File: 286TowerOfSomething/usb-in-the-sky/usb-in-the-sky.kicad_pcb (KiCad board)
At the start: 2 copper layers, 105.8 x 65.9 mm, 27 parts, among them J1 Bus_ISA_8bit, J2 USB_A, SW1 SW_DIP_x05, U1 CH375, U2 74LS688, U3 74LS245, U4 74ALS688, U5 SST39SF010, U6 USBLC6-2SC6, Y1 12 MHz

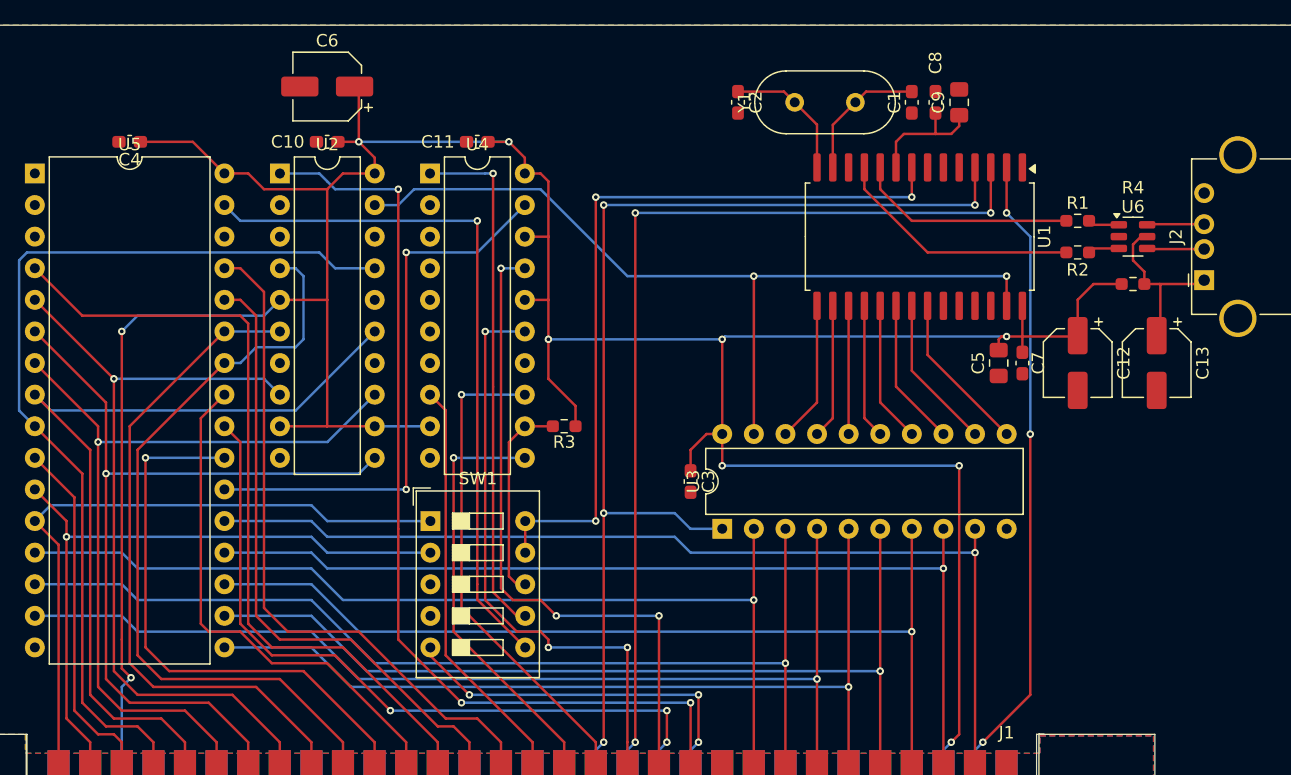
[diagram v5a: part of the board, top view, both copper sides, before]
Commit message: Work on USB in the Sky silkscreen
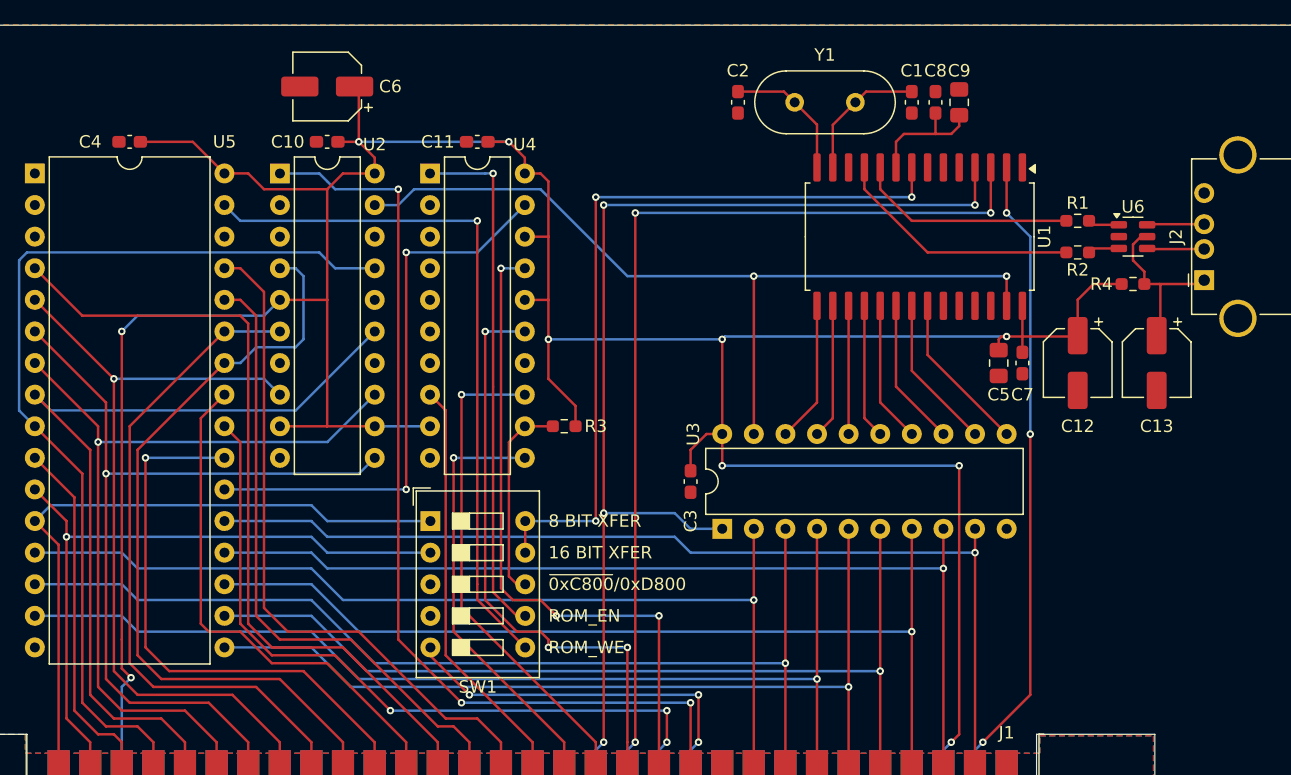
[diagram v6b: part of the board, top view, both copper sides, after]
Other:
- board text added: "16 BIT XFER"
- board text added: "8 BIT XFER"
- board text added: "ROM_EN"
- board text added: "ROM_WE"
- board text added: "~{0xC800}/0xD800"
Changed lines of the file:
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@@
 		(tags "capacitor electrolytic")
 		(property "Reference" "C12"
-			(at 0 -3.7 90)
+			(at 5.08 0 180)
 			(layer "F.SilkS")
 			(effects
@@
 		(tags "DIP Switch SPST Slide 7.62mm 300mil")
 		(property "Reference" "SW1"
-			(at 3.81 -3.42 0)
+			(at 3.81 13.33 0)
 			(layer "F.SilkS")
 			(effects
@@
 		(tags "resistor handsolder")
 		(property "Reference" "R3"
-			(at 0 -1.27 360)
+			(at -2.54 0 360)
 			(layer "F.SilkS")
 			(effects
@@
 		(tags "THT DIP DIL PDIP 2.54mm 15.24mm 600mil")
 		(property "Reference" "U5"
-			(at 7.62 -2.33 0)
+			(at 15.245 -2.54 0)
 			(layer "F.SilkS")
 			(effects
@@
 		(tags "capacitor handsolder")
 		(property "Reference" "C8"
-			(at 3.175 0 90)
+			(at 2.54 0 180)
 			(layer "F.SilkS")
 			(effects
@@
 		(tags "capacitor handsolder")
 		(property "Reference" "C1"
-			(at 0 1.397 90)
+			(at -2.54 0 0)
 			(layer "F.SilkS")
 			(effects
@@
 		(tags "capacitor handsolder")
 		(property "Reference" "C4"
-			(at 0 -1.43 360)
+			(at 3.175 0 360)
 			(layer "F.SilkS")
 			(effects
@@
 		(tags "capacitor handsolder")
 		(property "Reference" "C3"
-			(at 0 -1.43 90)
+			(at 3.175 0 90)
 			(layer "F.SilkS")
 			(effects
@@
 		(tags "THT DIP DIL PDIP 2.54mm 7.62mm 300mil")
 		(property "Reference" "U3"
-			(at 3.81 -2.33 90)
+			(at 7.61 -2.33 90)
 			(layer "F.SilkS")
 			(effects
@@
 		(tags "THT DIP DIL PDIP 2.54mm 7.62mm 300mil")
 		(property "Reference" "U2"
-			(at 3.81 -2.33 0)
+			(at 7.61 -2.33 0)
 			(layer "F.SilkS")
 			(effects
@@
 		(tags "resistor handsolder")
 		(property "Reference" "R4"
-			(at 0 -7.747 0)
+			(at -2.54 0 0)
 			(layer "F.SilkS")
 			(effects
@@
 		(tags "THT DIP DIL PDIP 2.54mm 7.62mm 300mil")
 		(property "Reference" "U4"
-			(at 3.81 -2.33 0)
+			(at 7.61 -2.33 0)
 			(layer "F.SilkS")
 			(effects
@@
 		(tags "THT crystalHC-49/U")
 		(property "Reference" "Y1"
-			(at 8.927 0 90)
+			(at 2.45 3.81 180)
 			(layer "F.SilkS")
 			(effects
@@
 		(tags "capacitor handsolder")
 		(property "Reference" "C9"
-			(at 0 -1.68 90)
+			(at 2.54 0 180)
 			(layer "F.SilkS")
 			(effects
@@
 		(tags "capacitor handsolder")
 		(property "Reference" "C2"
-			(at 0 -1.43 90)
+			(at -2.54 0 180)
 			(layer "F.SilkS")
 			(effects
@@
 		(tags "capacitor electrolytic")
 		(property "Reference" "C6"
-			(at 0 3.683 0)
+			(at -5.08 0 0)
 			(layer "F.SilkS")
 			(effects
@@
 		(tags "capacitor handsolder")
 		(property "Reference" "C5"
-			(at 0 1.651 90)
+			(at 2.54 0 180)
 			(layer "F.SilkS")
 			(effects
@@
 		(tags "capacitor handsolder")
 		(property "Reference" "C7"
-			(at 0 -1.27 90)
+			(at 2.54 0 180)
 			(layer "F.SilkS")
 			(effects
@@
 		(tags "capacitor electrolytic")
 		(property "Reference" "C13"
-			(at 0 -3.7 90)
+			(at 5.08 0 180)
 			(layer "F.SilkS")
 			(effects
@@
 		(layer "F.Fab")
 	)
+	(gr_text "~{0xC800}/0xD800"
+		(at 125.73 114.935 0)
+		(layer "F.SilkS" knockout)
+		(effects
+			(font
+				(size 1 1)
+				(thickness 0.1)
+			)
+			(justify left)
+		)
+	)
+	(gr_text "8 BIT XFER"
+		(at 125.73 109.855 0)
+		(layer "F.SilkS" knockout)
+		(effects
+			(font
+				(size 1 1)
+				(thickness 0.1)
+			)
+			(justify left)
+		)
+	)
+	(gr_text "16 BIT XFER"
+		(at 125.73 112.395 0)
+		(layer "F.SilkS" knockout)
+		(effects
+			(font
+				(size 1 1)
+				(thickness 0.1)
+			)
+			(justify left)
+		)
+	)
+	(gr_text "ROM_WE"
+		(at 125.73 120.015 0)
+		(layer "F.SilkS" knockout)
+		(effects
+			(font
+				(size 1 1)
+				(thickness 0.1)
+			)
+			(justify left)
+		)
+	)
+	(gr_text "ROM_EN"
+		(at 125.73 117.475 0)
+		(layer "F.SilkS" knockout)
+		(effects
+			(font
+				(size 1 1)
+				(thickness 0.1)
+			)
+			(justify left)
+		)
+	)
 	(dimension

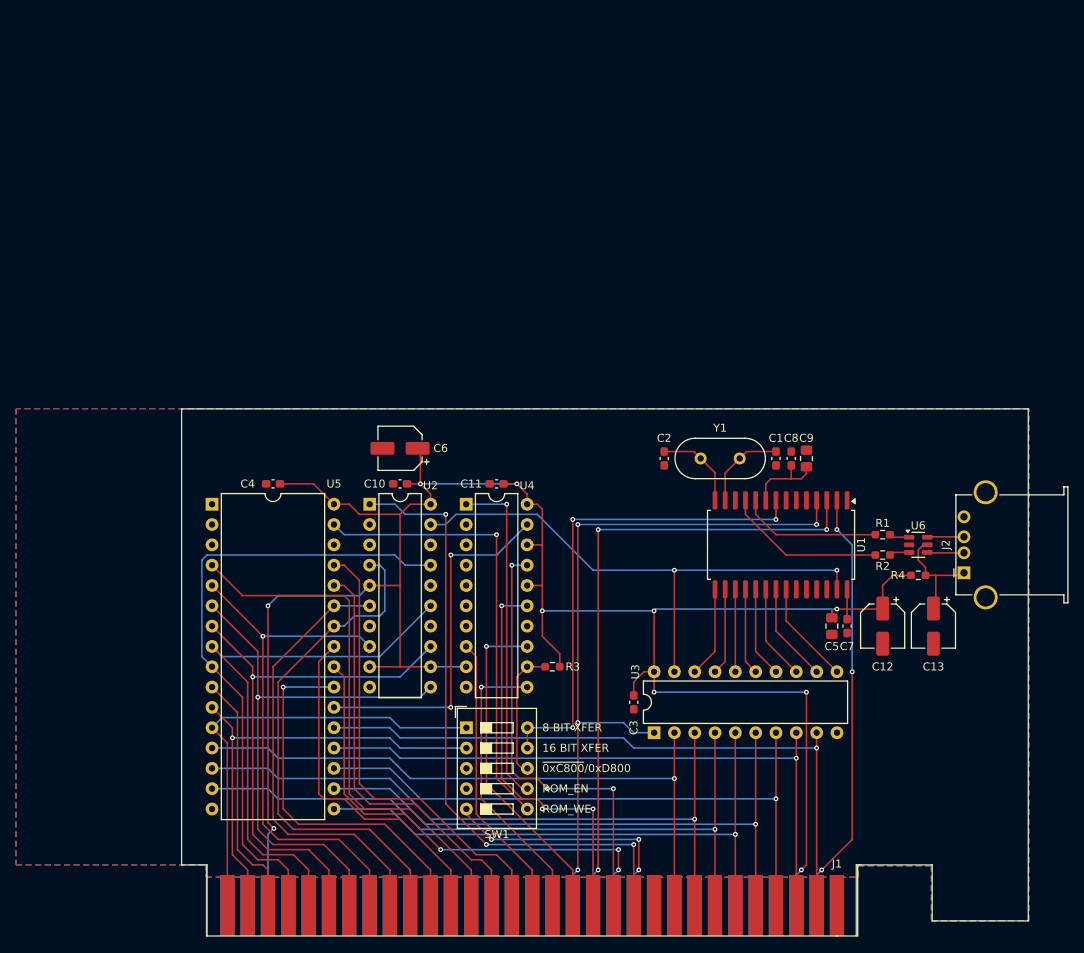
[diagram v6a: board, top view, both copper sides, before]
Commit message: Adding bracket to USB card
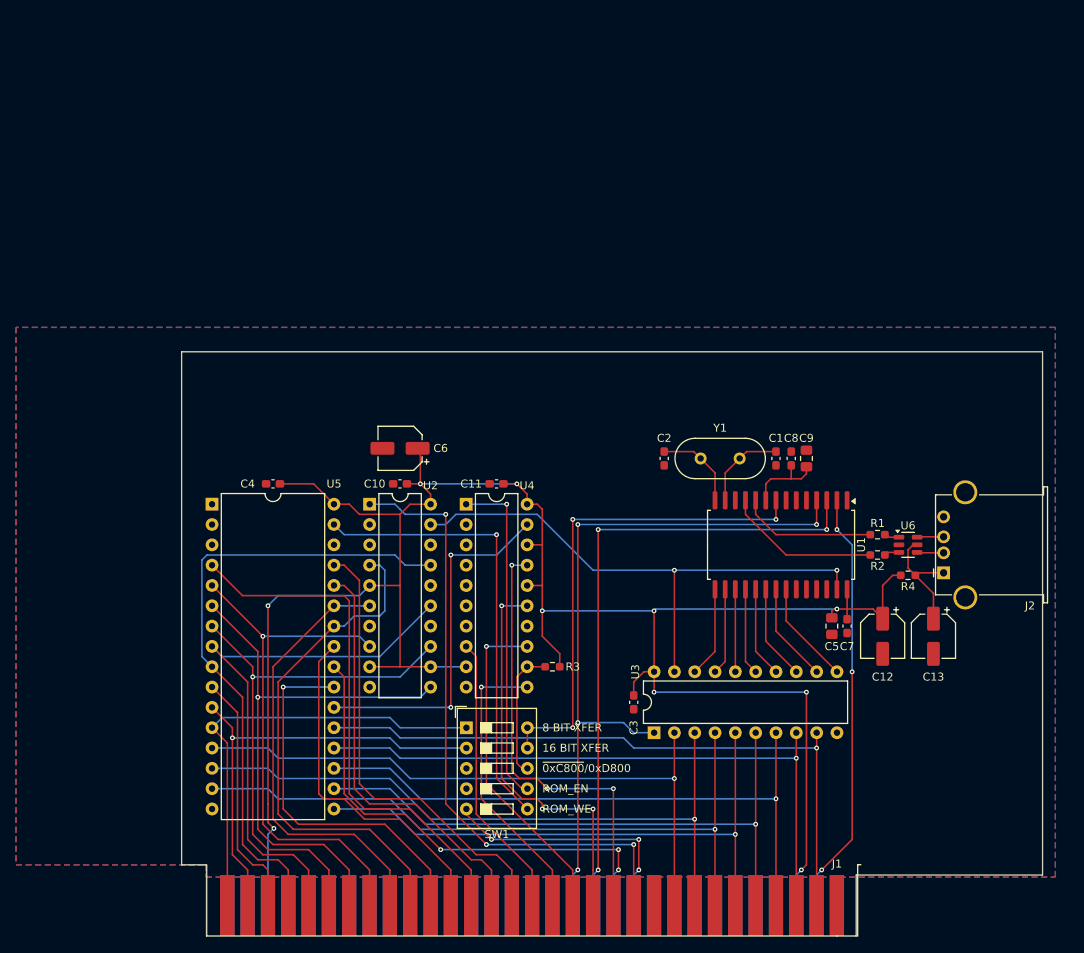
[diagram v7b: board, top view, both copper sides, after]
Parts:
- added BRACKET1: ~, pc-parts:PC_BRACKET_ISA_KEYSTONE_9200_Rev1_1, F.Cu at (162.6, 135.9)
- moved J2 2.55 mm to (175.9, 90.5)
- moved R4 1.27 mm to (171.4, 90.8)
- moved U6 1.27 mm to (171.4, 87.0)
- moved C12 1.27 mm to (168.3, 98.4)
- moved C13 1.27 mm to (174.6, 98.4)
- moved R1 0.64 mm to (167.6, 85.7)
- moved R2 0.64 mm to (167.6, 88.3)
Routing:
- net Net-(J2-D-): track 4.61 -> 3.33 mm
- net Net-(J2-D+): track 4.61 -> 3.33 mm
- net Net-(U1-UD-): track 20.1 -> 19.5 mm
- net Net-(U1-UD+): track 17.8 -> 17.1 mm
- net Net-(R2-Pad2): track 2.53 -> 1.89 mm
- net Net-(R1-Pad2): track 2.53 -> 1.89 mm
- net Net-(J2-VBUS): track 14.4 -> 15.0 mm
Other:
- board size 105.8 x 65.9 mm -> 107.6 x 73 mm
